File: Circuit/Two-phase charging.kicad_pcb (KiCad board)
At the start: 2 copper layers, 80 x 60 mm, 73 parts, among them IC1 MCP6541, IC2 V7805-500, IC3 SI8261BAC-C-IP, IC4 TMR1-0522, IC5 MCP6542, IC6 ATTINY84-20PU, J1 Power connector, J2 CAR, J3 Mount, J4 Mount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

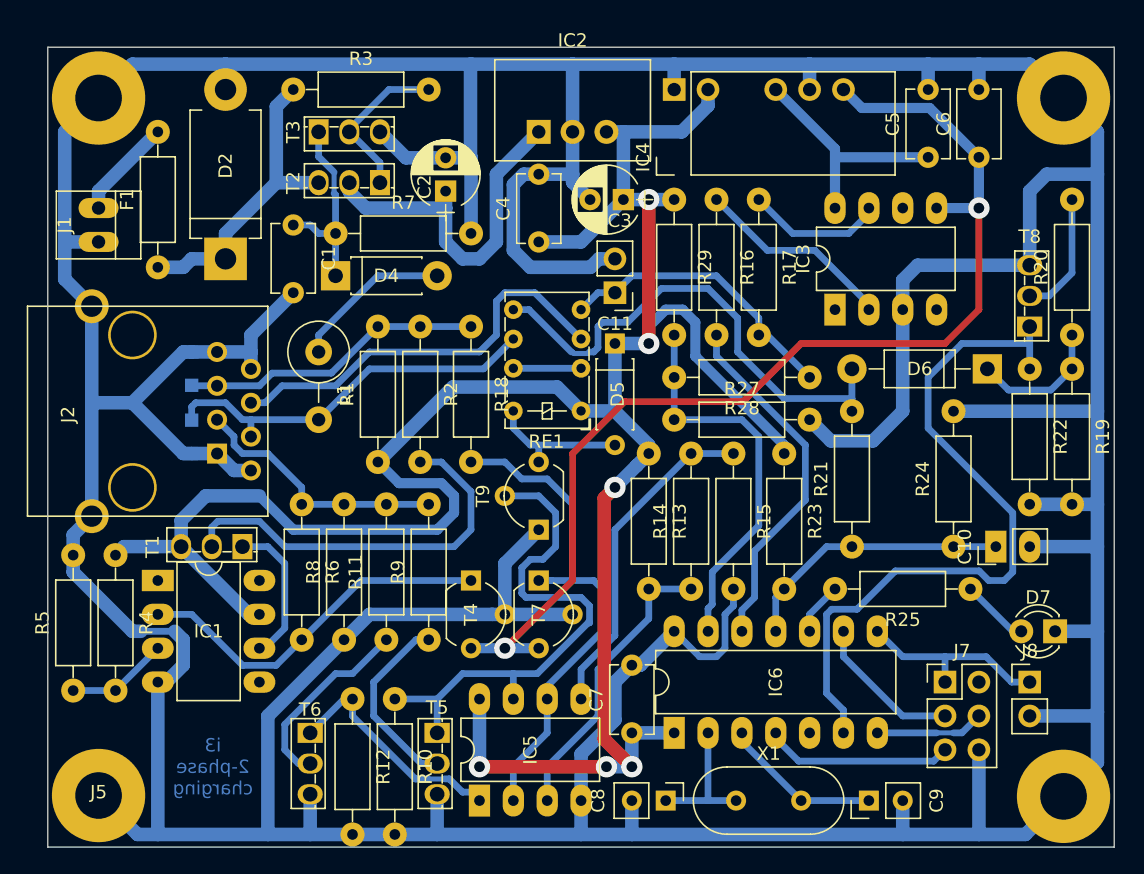
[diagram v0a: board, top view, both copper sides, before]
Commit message: Some PCB layout improvements
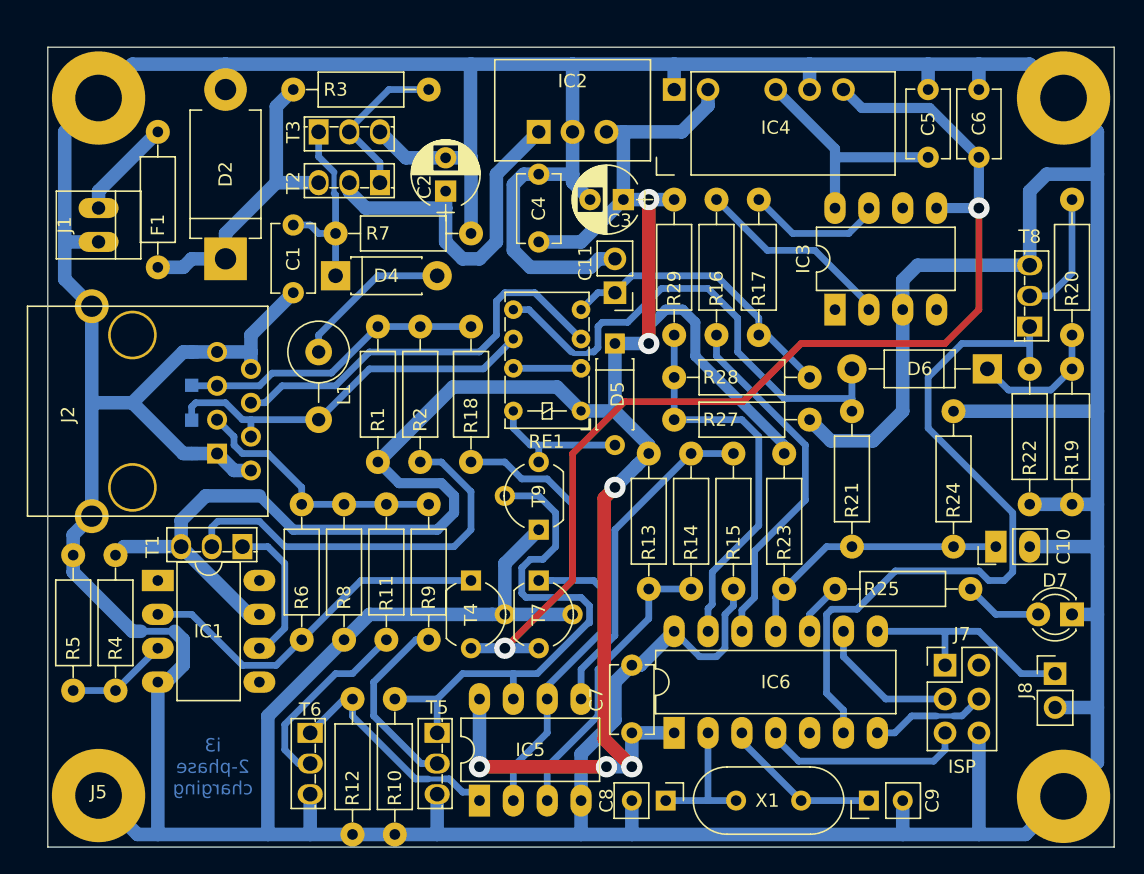
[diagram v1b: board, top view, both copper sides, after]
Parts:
- moved J8 2.01 mm to (151.8, 97.8)
- moved D7 1.80 mm to (153.0, 93.3)
- moved J7 1.27 mm to (143.5, 97.2)
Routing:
- net /MISO: track 14.9 -> 17.2 mm
- net GND: track 517.5 -> 515.5 mm
- net /RESET: track 14.2 -> 15.4 mm
- net Net-(D7-Pad2): track 5.13 -> 5.87 mm
- net /MOSI: track 8.15 -> 8.67 mm
- net /SCK: track 11.4 -> 10.8 mm
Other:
- board text added: "ISP"
